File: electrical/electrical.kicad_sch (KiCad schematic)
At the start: 25 parts, among them J1 Raspberry Pi GPIO, J10 power sesor, J11 vibration motor, J12 Conn_01x02_Pin, J13 Conn_01x02_Pin, J14 cup sensor, J2 Load_cell, J3 Pump_driver, J4 PIR_sensor, J5 Load_cell, J6 Milk_powder_sensor, J7 Instant_coffee_sensor, J8 Sugar_sensor, J9 Water_sensor, K1 Heater_relay, M1 Milk_powder, M2 Instant_coffee, M3 Sugar, Q1 IRLZ44N, Q2 IRLZ44N, Q3 IRLZ44N, SW1 Thermostat

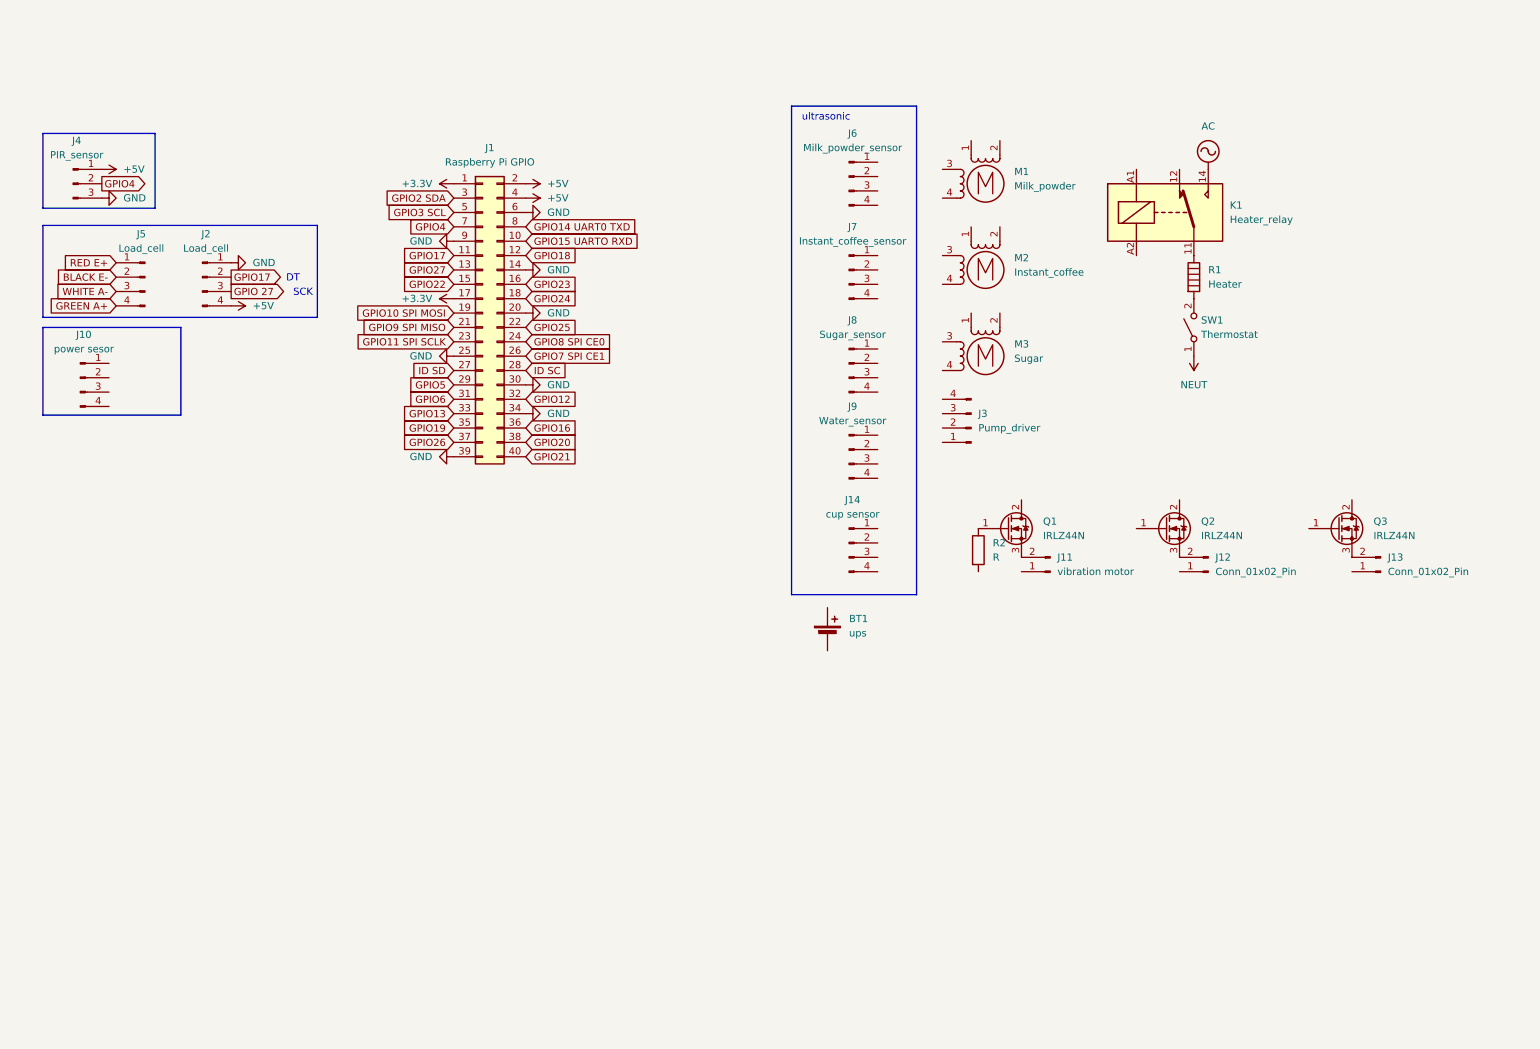
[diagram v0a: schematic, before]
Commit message: added notification url
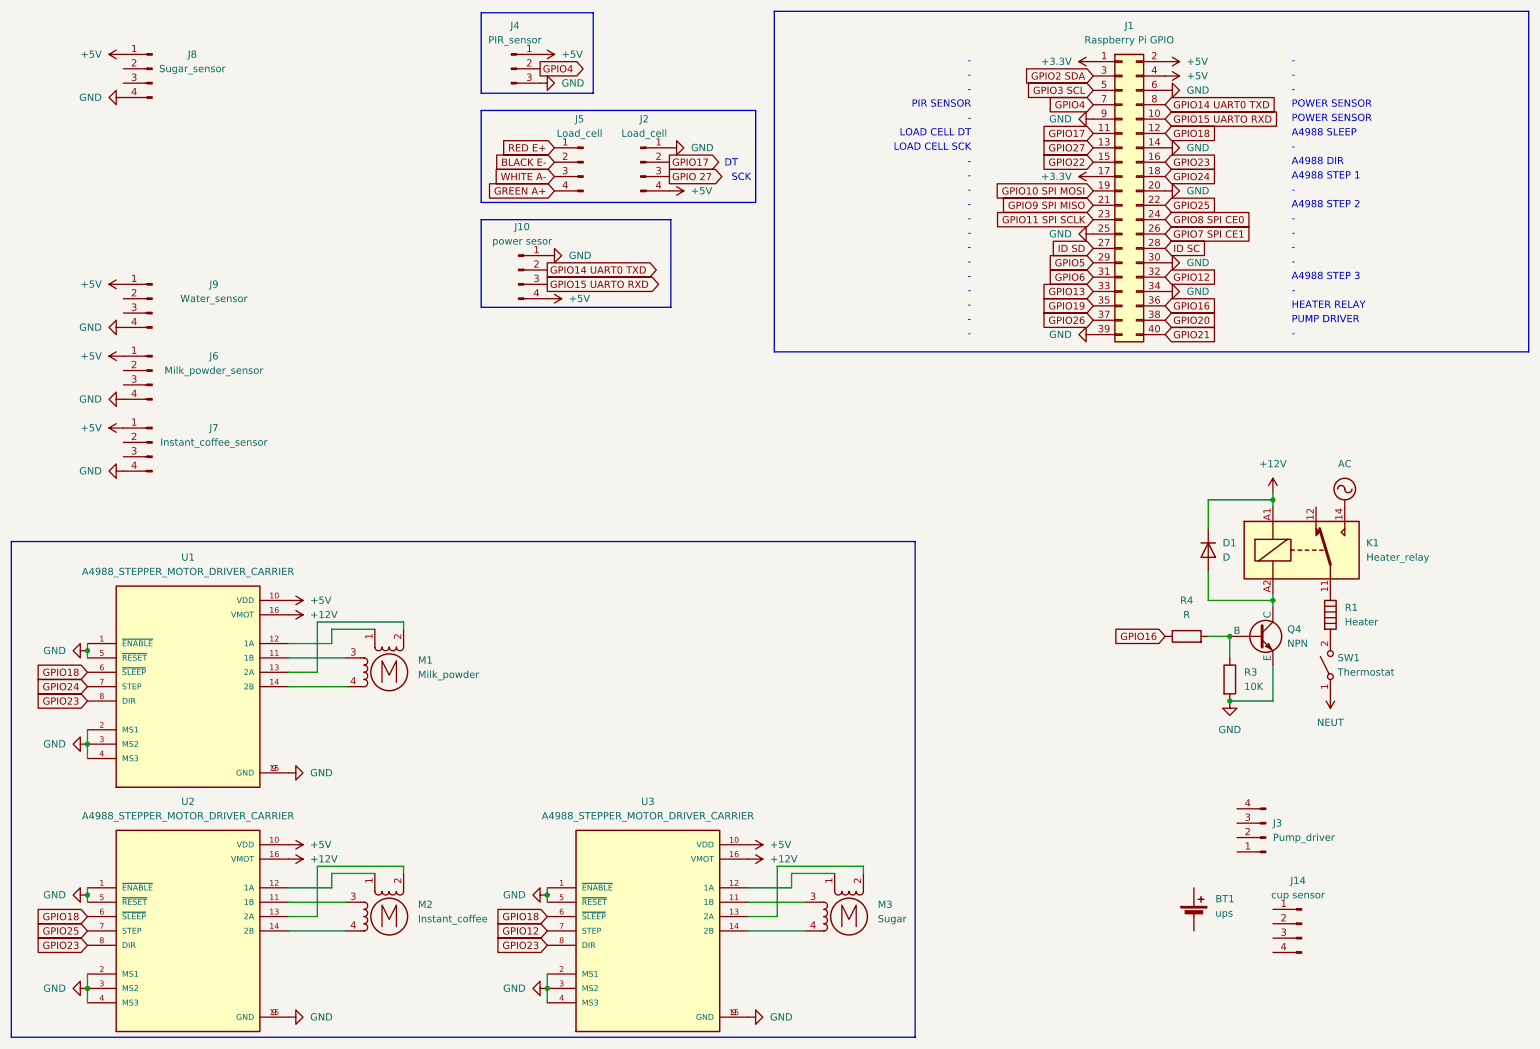
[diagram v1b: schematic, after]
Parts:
- removed J11: vibration motor, symbol Connector:Conn_01x02_Pin
- removed J12, J13: Conn_01x02_Pin, symbol Connector:Conn_01x02_Pin
- removed Q1, Q2, Q3: IRLZ44N, Package_TO_SOT_THT:TO-220-3_Vertical, symbol Transistor_FET:IRLZ44N
- removed R2: R, symbol Device:R
- added D1: D, symbol Device:D
- added Q4: NPN, symbol Simulation_SPICE:NPN
- added R3: 10K, symbol Device:R
- added R4: R, symbol Device:R
- added U1, U2, U3: A4988_STEPPER_MOTOR_DRIVER_CARRIER, A4988_STEPPER_MOTOR_DRIVER_CARRIER:MODULE_A4988_STEPPER_MOTOR_DRIVER_CARRIER, symbol A4988_STEPPER_MOTOR_DRIVER_CARRIER:A4988_STEPPER_MOTOR_DRIVER_CARRIER
- J6, J7, J8, J9: footprint (none) -> Connector_PinHeader_2.54mm:PinHeader_1x04_P2.54mm_Vertical
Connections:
- net +5V: now also J10.4 (Pin_4), J6.1 (Pin_1), J7.1 (Pin_1), J8.1 (Pin_1), J9.1 (Pin_1), U1.10 (VDD), U2.10 (VDD), U3.10 (VDD)
- net GND: now also J10.1 (Pin_1), J6.4 (Pin_4), J7.4 (Pin_4), J8.4 (Pin_4), J9.4 (Pin_4), Q4.3 (E), R3.2, U1.1 (~{ENABLE}), U1.15 (GND), U1.2 (MS1), U1.3 (MS2), U1.4 (MS3), U1.5 (~{RESET}), U1.9 (GND), U2.1 (~{ENABLE}), U2.15 (GND), U2.2 (MS1), U2.3 (MS2), U2.4 (MS3), U2.5 (~{RESET}), U2.9 (GND), U3.1 (~{ENABLE}), U3.15 (GND), U3.2 (MS1), U3.3 (MS2), U3.4 (MS3), U3.5 (~{RESET}), U3.9 (GND)
- net GPIO12: now also U3.7 (STEP)
- net GPIO14 UART0 TXD: now also J10.2 (Pin_2)
- net GPIO15 UARTO RXD: now also J10.3 (Pin_3)
- net GPIO16: now also R4.1
- net GPIO18: now also U1.6 (~{SLEEP}), U2.6 (~{SLEEP}), U3.6 (~{SLEEP})
- net GPIO23: now also U1.8 (DIR), U2.8 (DIR), U3.8 (DIR)
- net GPIO24: now also U1.7 (STEP)
- net GPIO25: now also U2.7 (STEP)
- net +12V: now reaches K1.A1
- net +12V: now also D1.1 (K), U1.16 (VMOT), U2.16 (VMOT), U3.16 (VMOT)
- net at K1.A2: now also D1.2 (A), Q4.1 (C)
- net at M2.1: now also U2.12 (1A)
- net at M2.2 (-): now also U2.13 (2A)
- net at M2.3: now also U2.11 (1B)
- net at M2.4: now also U2.14 (2B)
- net at M1.1: now also U1.12 (1A)
- net at M1.2 (-): now also U1.13 (2A)
- net at M1.3: now also U1.11 (1B)
- net at M1.4: now also U1.14 (2B)
- net at M3.1: now also U3.12 (1A)
- net at M3.2 (-): now also U3.13 (2A)
- net at M3.3: now also U3.11 (1B)
- net at M3.4: now also U3.14 (2B)
- new net: Q4.2 (B), R3.1, R4.2
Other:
- note added: "-"
- note added: "A4988 DIR"
- note added: "A4988 SLEEP"
- note added: "A4988 STEP 1"
- note added: "A4988 STEP 2"
- note added: "A4988 STEP 3"
- note added: "HEATER RELAY"
- note added: "LOAD CELL DT"
- note added: "LOAD CELL SCK"
- note added: "PIR SENSOR"
- note added: "POWER SENSOR"
- note added: "PUMP DRIVER"
- note removed: "ultrasonic"
- moved on the sheet: BT1, J1, J10, J14, J2, J3, J4, J5, J6, J7, J8, J9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

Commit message: idk
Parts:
- removed BT1: ups, symbol Device:Battery_Cell
- removed J10: power sesor, symbol Connector:Conn_01x04_Pin
- removed J14: cup sensor, symbol Connector:Conn_01x04_Pin
- removed J2, J5: Load_cell, symbol Connector:Conn_01x04_Pin
- removed J6: Milk_powder_sensor, Connector_PinHeader_2.54mm:PinHeader_1x04_P2.54mm_Vertical, symbol Connector:Conn_01x04_Pin
- removed J7: Instant_coffee_sensor, Connector_PinHeader_2.54mm:PinHeader_1x04_P2.54mm_Vertical, symbol Connector:Conn_01x04_Pin
- removed J8: Sugar_sensor, Connector_PinHeader_2.54mm:PinHeader_1x04_P2.54mm_Vertical, symbol Connector:Conn_01x04_Pin
- removed K1: Heater_relay, symbol Relay:Relay_SPDT
- added D6: LED, LED_THT:LED_D3.0mm, symbol Device:LED
- added K1: RAYEX-L90, Relay_THT:Relay_SPDT_RAYEX-L90, symbol Relay:RAYEX-L90
- added M4: Motor_DC, TerminalBlock_Phoenix:TerminalBlock_Phoenix_MKDS-1,5-2-5.08_1x02_P5.08mm_Horizontal, symbol Motor:Motor_DC
- added P1: IEC_60320_C13_Plug, TerminalBlock_Phoenix:TerminalBlock_Phoenix_MKDS-1,5-2-5.08_1x02_P5.08mm_Horizontal, symbol Connector:IEC_60320_C13_Plug
- added Q1: 2N3904, Package_TO_SOT_THT:TO-92_Inline_Wide, symbol Simulation_SPICE:NPN
- added R10, R9: 10K, Resistor_SMD:R_1206_3216Metric_Pad1.30x1.75mm_HandSolder, symbol Device:R
- added R8: 510, Resistor_SMD:R_1206_3216Metric_Pad1.30x1.75mm_HandSolder, symbol Device:R
- added SW2: SW_SPDT, Button_Switch_THT:SW_NKK_G1xJP, symbol Switch:SW_SPDT
- added U5: PC817, Package_DIP:DIP-4_W7.62mm_LongPads, symbol Isolator:PC817
- added U7: ~, Library:HX711, symbol hx711:hx711
- added e1: IRF540N, Package_TO_SOT_SMD:TO-263-2, symbol Transistor_FET:IRF540N
- D1: value D -> 1N4007; footprint (none) -> Diode_THT:D_5W_P12.70mm_Horizontal
- J3: value Pump_driver -> Load_cell; footprint (none) -> Connector_PinHeader_2.54mm:PinHeader_1x04_P2.54mm_Vertical
- J4: footprint (none) -> Connector_PinSocket_2.54mm:PinSocket_1x03_P2.54mm_Vertical
- Q4: value NPN -> 2N3904; footprint (none) -> Package_TO_SOT_THT:TO-92_Inline_Wide
- R1: footprint (none) -> TerminalBlock_Phoenix:TerminalBlock_Phoenix_MKDS-1,5-2-5.08_1x02_P5.08mm_Horizontal
- R3: value 10K -> 120; footprint (none) -> Resistor_SMD:R_1206_3216Metric_Pad1.30x1.75mm_HandSolder
- R4: value R -> 470; footprint (none) -> Resistor_SMD:R_1206_3216Metric_Pad1.30x1.75mm_HandSolder
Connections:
- net +12V: now also K1.A1, M4.1 (+), R10.1, R8.1, U5.4
- net +5V: now also U7.4 (VCC)
- net AC: now also P1.2 (L), SW2.2 (B)
- net BLACK E-: now also J3.2 (Pin_2), U7.8 (A+)
- net GND: now also U5.2, U7.1 (GND); no longer Q4.3 (E), R3.2
- net GPIO17: now also U7.2 (DATA)
- net GPIO27: now also U7.3 (SCK)
- net GREEN A+: now also J3.4 (Pin_4), U7.10 (B+)
- net NEUT: now also R1.2, SW1.2 (B), P1.1 (N)
- net RED E+: now also J3.1 (Pin_1), U7.7 (A-)
- net WHITE A-: now also J3.3 (Pin_3), U7.9 (B-)
- net at R1.1: now also K1.11A, K1.11B
- net at D1.2 (A), Q4.1 (C): now also D6.1 (K), K1.A2
- net at M2.1: now also U2.11 (1B); no longer U2.12 (1A)
- net at M2.2 (-): now also U2.12 (1A); no longer U2.13 (2A)
- net at M2.3: now also U2.13 (2A); no longer U2.11 (1B)
- net at U3.11 (1B): now also M3.1; no longer M3.3
- net at U3.12 (1A): now also M3.2 (-); no longer M3.1
- net at U3.13 (2A): now also M3.3; no longer M3.2 (-)
- net at U1.11 (1B): now also M1.1; no longer M1.3
- net at U1.12 (1A): now also M1.2 (-); no longer M1.1
- net at U1.13 (2A): now also M1.3; no longer M1.2 (-)
- net GPIO14 UART0 TXD: no longer names the net of J1.8 (Pin_8)
- net GPIO15 UARTO RXD: no longer names the net of J1.10 (Pin_10)
- new net: M4.2 (-), e1.2 (D)
- new net: K1.14, SW2.1 (A)
- new net: K1.12, SW2.3 (C)
- new net: R3.1, U5.3
- new net: Q4.2 (B), R3.2
- new net: Q1.1 (C), R10.2, e1.1 (G)
- new net: R4.2, U5.1
- new net: D6.2 (A), R8.2
- new net: Q1.2 (B), R9.1
- new net GND +12V: Q1.3 (E), Q4.3 (E), e1.3 (S)
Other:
- added sheet Untitled Sheet1 (untitled.kicad_sch)
- added sheet Untitled Sheet2 (untitled.kicad_sch)
- note removed: "POWER SENSOR"
- moved on the sheet: D1, J1, J4, J9, M1, M2, M3, Q4, R1, R3, R4, SW1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
